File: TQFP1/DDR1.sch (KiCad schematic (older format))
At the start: 19 parts, among them U2 MT46V32M16TG, U3 M25P32

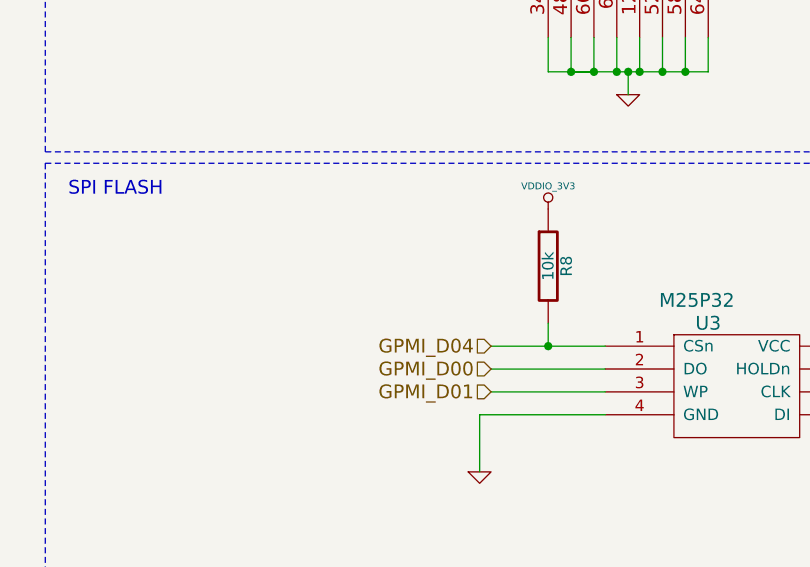
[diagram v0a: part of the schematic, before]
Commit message: PCB labels, improvements 15/04/11
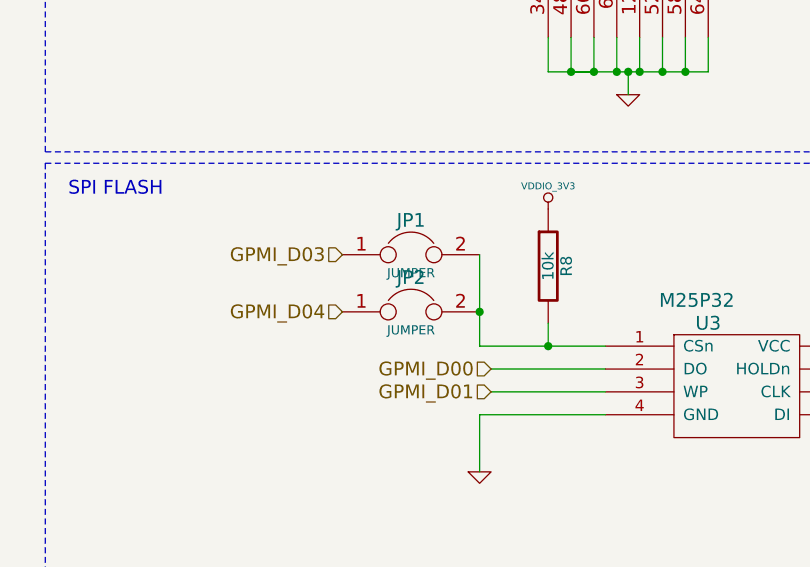
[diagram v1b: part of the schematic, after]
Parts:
- added JP1, JP2: JUMPER, symbol JUMPER
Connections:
- net labels added: GPMI_D03
- wire segments 137 -> 138
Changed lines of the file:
@@
-EESchema Schematic File Version 2  date Mon 11 Apr 2011 03:43:24 PM COT
+EESchema Schematic File Version 2  date Fri 15 Apr 2011 03:10:43 PM COT
+LIBS:con-jack
 LIBS:adm3101e
 LIBS:microsd
@@
 Sheet 2 3
 Title ""
-Date "11 apr 2011"
+Date "15 apr 2011"
 Rev ""
 Comp ""
@@
 Comment4 ""
 $EndDescr
+Connection ~ 7650 6000
+Wire Wire Line
+	8200 6150 7650 6150
+Wire Wire Line
+	7650 6150 7650 5750
 Connection ~ 7950 6150
 Wire Wire Line
@@
 Wire Wire Line
 	7700 6350 8200 6350
-Wire Wire Line
-	7700 6150 8200 6150
 Connection ~ 8550 1500
 Connection ~ 8350 1500
@@
 Wire Wire Line
 	5850 3800 7250 3800
+Text HLabel 7050 5750 0    60   Input ~ 0
+GPMI_D03
+$Comp
+L JUMPER JP2
+U 1 1 4DA8641E
+P 7350 6000
+F 0 "JP2" H 7350 6150 60  0000 C CNN
+F 1 "JUMPER" H 7350 5920 40  0000 C CNN
+	1    7350 6000
+	1    0    0    -1
+$EndComp
+$Comp
+L JUMPER JP1
+U 1 1 4DA8641B
+P 7350 5750
+F 0 "JP1" H 7350 5900 60  0000 C CNN
+F 1 "JUMPER" H 7350 5670 40  0000 C CNN
+	1    7350 5750
+	1    0    0    -1
+$EndComp
 $Comp
 L VDDIO_3V3 #PWR01
@@
 Text HLabel 7700 6250 0    60   Input ~ 0
 GPMI_D00
-Text HLabel 7700 6150 0    60   Input ~ 0
+Text HLabel 7050 6000 0    60   Input ~ 0
 GPMI_D04
 $Comp

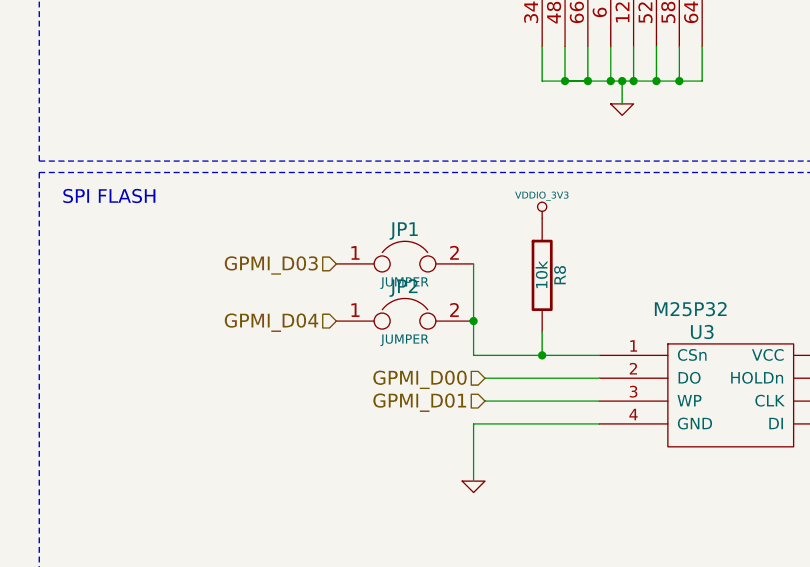
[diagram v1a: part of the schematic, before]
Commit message: Some PCB and boot changes
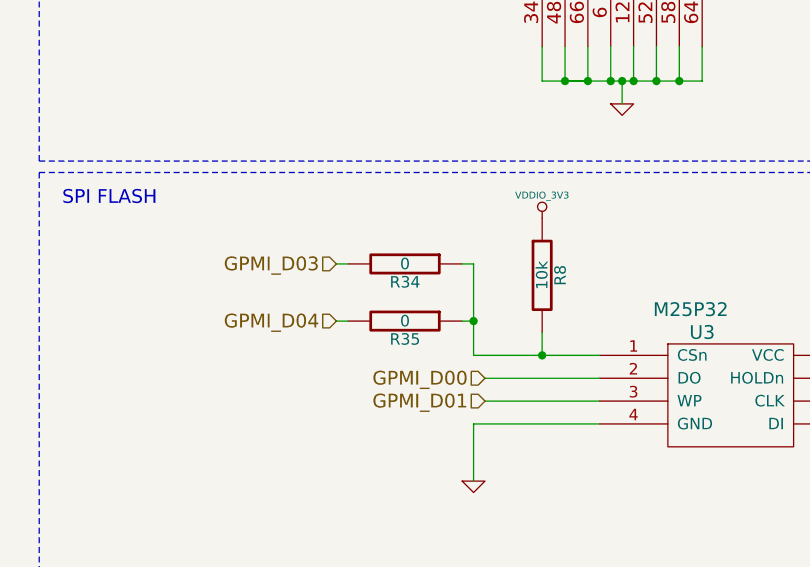
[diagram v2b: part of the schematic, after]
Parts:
- removed JP1, JP2: JUMPER, symbol JUMPER
- added R34, R35: 0, symbol R
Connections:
- wire segments 138 -> 142
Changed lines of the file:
@@
-EESchema Schematic File Version 2  date Fri 15 Apr 2011 03:10:43 PM COT
-LIBS:con-jack
-LIBS:adm3101e
-LIBS:microsd
-LIBS:transistor-npn
-LIBS:ipc-7351-transistor
-LIBS:switch-misc
+EESchema Schematic File Version 2  date Thu 21 Apr 2011 06:26:39 PM COT
 LIBS:power
 LIBS:device
@@
 LIBS:contrib
 LIBS:valves
-LIBS:micron_ddr_512Mb
-LIBS:iMX23
-LIBS:sdmmc
-LIBS:usbconn
-LIBS:fsusb20
-LIBS:r_pack2
-LIBS:pasives-connectors
-LIBS:EEPROM
-LIBS:PWR
-LIBS:m25p32
-LIBS:PROpendous-cache
-LIBS:w_analog
 LIBS:i.mx233stamp-cache
 EELAYER 25  0
@@
 Sheet 2 3
 Title ""
-Date "15 apr 2011"
+Date "21 apr 2011"
 Rev ""
 Comp ""
@@
 Comment4 ""
 $EndDescr
+Wire Wire Line
+	7050 6000 7100 6000
+Wire Wire Line
+	7600 5750 7650 5750
 Connection ~ 7650 6000
 Wire Wire Line
@@
 Wire Wire Line
 	5850 3800 7250 3800
+Wire Wire Line
+	7050 5750 7100 5750
+Wire Wire Line
+	7600 6000 7650 6000
+$Comp
+L R R35
+U 1 1 4DACFF24
+P 7350 6000
+F 0 "R35" V 7430 6000 50  0000 C CNN
+F 1 "0" V 7350 6000 50  0000 C CNN
+	1    7350 6000
+	0    1    1    0
+$EndComp
+$Comp
+L R R34
+U 1 1 4DACFF20
+P 7350 5750
+F 0 "R34" V 7430 5750 50  0000 C CNN
+F 1 "0" V 7350 5750 50  0000 C CNN
+	1    7350 5750
+	0    1    1    0
+$EndComp
 Text HLabel 7050 5750 0    60   Input ~ 0
 GPMI_D03
 $Comp
-L JUMPER JP2
-U 1 1 4DA8641E
-P 7350 6000
-F 0 "JP2" H 7350 6150 60  0000 C CNN
-F 1 "JUMPER" H 7350 5920 40  0000 C CNN
-	1    7350 6000
-	1    0    0    -1
-$EndComp
-$Comp
-L JUMPER JP1
-U 1 1 4DA8641B
-P 7350 5750
-F 0 "JP1" H 7350 5900 60  0000 C CNN
-F 1 "JUMPER" H 7350 5670 40  0000 C CNN
-	1    7350 5750
-	1    0    0    -1
-$EndComp
-$Comp
-L VDDIO_3V3 #PWR01
+L VDDIO_3V3 #PWR6
 U 1 1 4D7E71FF
 P 7950 5550
-F 0 "#PWR01" H 7950 5650 30  0001 C CNN
+F 0 "#PWR6" H 7950 5650 30  0001 C CNN
 F 1 "VDDIO_3V3" H 7950 5650 30  0000 C CNN
 	1    7950 5550
@@
 $EndComp
 $Comp
-L VDDM_2V5 #PWR02
+L VDDM_2V5 #PWR2
 U 1 1 4D7E6BF9
 P 6000 3900
-F 0 "#PWR02" H 6000 4000 30  0001 C CNN
+F 0 "#PWR2" H 6000 4000 30  0001 C CNN
 F 1 "VDDM_2V5" H 5950 3950 30  0000 C CNN
 	1    6000 3900
@@
 $EndComp
 $Comp
-L GND #PWR03
+L GND #PWR1
 U 1 1 4D418353
 P 5850 4500
-F 0 "#PWR03" H 5850 4500 30  0001 C CNN
+F 0 "#PWR1" H 5850 4500 30  0001 C CNN
 F 1 "GND" H 5850 4430 30  0001 C CNN
 	1    5850 4500
@@
 DDR_CKE
 $Comp
-L GND #PWR04
+L GND #PWR13
 U 1 1 4D417AF1
 P 10800 2750
-F 0 "#PWR04" H 10800 2750 30  0001 C CNN
+F 0 "#PWR13" H 10800 2750 30  0001 C CNN
 F 1 "GND" H 10800 2680 30  0001 C CNN
 	1    10800 2750
@@
 $EndComp
 $Comp
-L VDDM_2V5 #PWR05
+L VDDM_2V5 #PWR12
 U 1 1 4D417ACD
 P 10800 1450
-F 0 "#PWR05" H 10800 1550 30  0001 C CNN
+F 0 "#PWR12" H 10800 1550 30  0001 C CNN
 F 1 "VDDM_2V5" H 10800 1550 30  0000 C CNN
 	1    10800 1450
@@
 $EndComp
 $Comp
-L VDDM_2V5 #PWR06
+L VDDM_2V5 #PWR3
 U 1 1 4D4179A4
 P 7250 800
-F 0 "#PWR06" H 7250 900 30  0001 C CNN
+F 0 "#PWR3" H 7250 900 30  0001 C CNN
 F 1 "VDDM_2V5" H 7250 900 30  0000 C CNN
 	1    7250 800
@@
 $EndComp
 $Comp
-L VDDM_2V5 #PWR07
+L VDDM_2V5 #PWR10
 U 1 1 4D417999
 P 10200 800
-F 0 "#PWR07" H 10200 900 30  0001 C CNN
+F 0 "#PWR10" H 10200 900 30  0001 C CNN
 F 1 "VDDM_2V5" H 10200 900 30  0000 C CNN
 	1    10200 800
@@
 $EndComp
 $Comp
-L GND #PWR08
+L GND #PWR4
 U 1 1 4D41792B
 P 7550 1500
-F 0 "#PWR08" H 7550 1500 30  0001 C CNN
+F 0 "#PWR4" H 7550 1500 30  0001 C CNN
 F 1 "GND" H 7550 1430 30  0001 C CNN
 	1    7550 1500
@@
 $EndComp
 $Comp
-L GND #PWR09
+L GND #PWR9
 U 1 1 4D417882
 P 9600 1500
-F 0 "#PWR09" H 9600 1500 30  0001 C CNN
+F 0 "#PWR9" H 9600 1500 30  0001 C CNN
 F 1 "GND" H 9600 1430 30  0001 C CNN
 	1    9600 1500
@@
 GPMI_D04
 $Comp
-L GND #PWR010
+L GND #PWR11
 U 1 1 4D409664
 P 10400 6050
-F 0 "#PWR010" H 10400 6050 30  0001 C CNN
+F 0 "#PWR11" H 10400 6050 30  0001 C CNN
 F 1 "GND" H 10400 5980 30  0001 C CNN
 	1    10400 6050
@@
 $EndComp
 $Comp
-L VDDIO_3V3 #PWR011
+L VDDIO_3V3 #PWR8
 U 1 1 4D409635
 P 9500 5950
-F 0 "#PWR011" H 9500 6050 30  0001 C CNN
+F 0 "#PWR8" H 9500 6050 30  0001 C CNN
 F 1 "VDDIO_3V3" H 9500 6050 30  0000 C CNN
 	1    9500 5950
@@
 $EndComp
 $Comp
-L GND #PWR012
+L GND #PWR5
 U 1 1 4D409619
 P 7650 6700
-F 0 "#PWR012" H 7650 6700 30  0001 C CNN
+F 0 "#PWR5" H 7650 6700 30  0001 C CNN
 F 1 "GND" H 7650 6630 30  0001 C CNN
 	1    7650 6700
@@
 DDR_WEN
 $Comp
-L GND #PWR013
+L GND #PWR7
 U 1 1 4D319D50
 P 8300 5050
-F 0 "#PWR013" H 8300 5050 30  0001 C CNN
+F 0 "#PWR7" H 8300 5050 30  0001 C CNN
 F 1 "GND" H 8300 4980 30  0001 C CNN
 	1    8300 5050
